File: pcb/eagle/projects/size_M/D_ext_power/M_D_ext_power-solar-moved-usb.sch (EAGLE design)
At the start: 30 parts

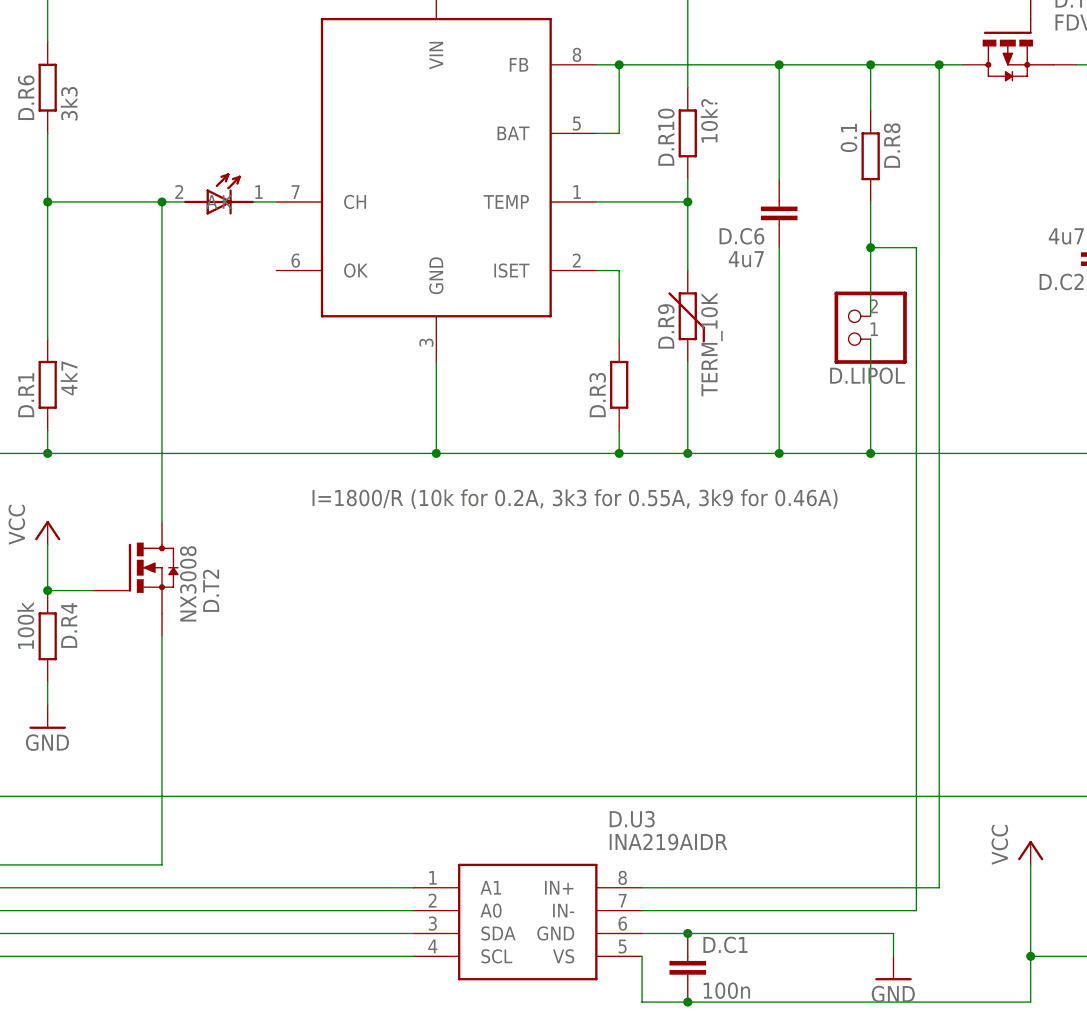
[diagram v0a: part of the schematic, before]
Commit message: LM3671_3.3 -> MCP1603T-330I attempt with  centered USB
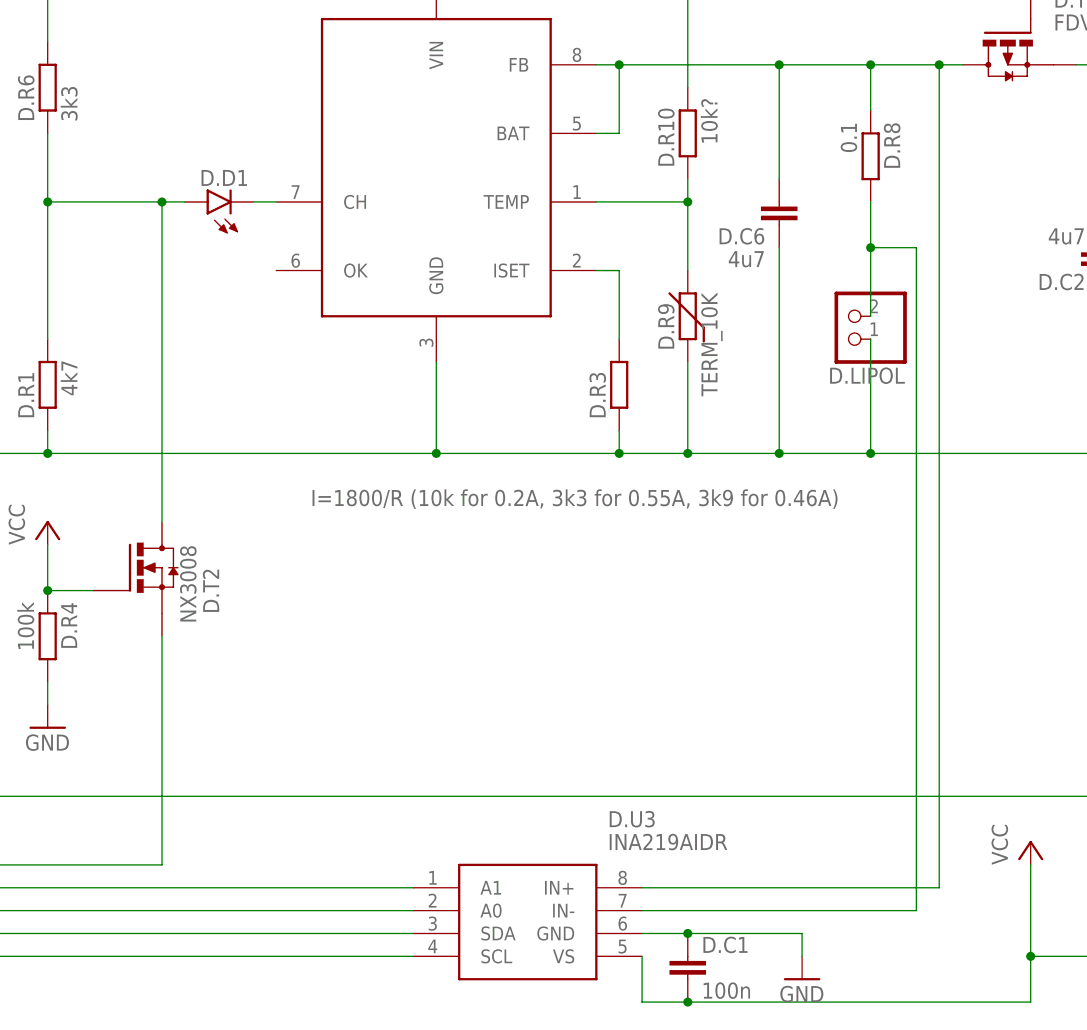
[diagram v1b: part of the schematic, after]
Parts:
- D.D1: value LED_1.8 -> (none); device hugo:LED_1.8 -> led:LEDCHIP-LED0603
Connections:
- net N$3: now also D.D1.C; no longer D.D1.K
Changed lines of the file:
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@@
 <part name="D.R6" library="rcl" library_urn="urn:adsk.eagle:library:334" deviceset="R-EU_" device="R0603" package3d_urn="urn:adsk.eagle:package:23555/3" value="3k3"/>
 <part name="D.R7" library="rcl" library_urn="urn:adsk.eagle:library:334" deviceset="R-EU_" device="R0603" package3d_urn="urn:adsk.eagle:package:23555/3" value="390k"/>
-<part name="D.D1" library="hugo" deviceset="LED_1.8" device=""/>
 <part name="D.L1" library="rcl" library_urn="urn:adsk.eagle:library:334" deviceset="L-EU" device="L3230M" package3d_urn="urn:adsk.eagle:package:23481/3" value="4u7"/>
 <part name="D.LIPOL" library="pinhead2" deviceset="PINHD-1X2" device="" package3d_urn="urn:adsk.eagle:package:22435/2"/>
@@
 <part name="U$2" library="hugo" deviceset="CN3083" device=""/>
 <part name="D.R10" library="rcl" library_urn="urn:adsk.eagle:library:334" deviceset="R-EU_" device="R0603" package3d_urn="urn:adsk.eagle:package:23555/3" value="10k?"/>
+<part name="D.D1" library="led" deviceset="LED" device="CHIP-LED0603" package3d_urn="urn:adsk.eagle:package:15819/3"/>
 </parts>
 <sheets>
@@
 <attribute name="VALUE" x="17.018" y="204.47" size="1.778" layer="96" rot="R270"/>
 </instance>
-<instance part="D.D1" gate="G$1" x="-88.9" y="190.5" smashed="yes"/>
 <instance part="D.L1" gate="G$1" x="71.12" y="205.74" smashed="yes" rot="R90">
 <attribute name="NAME" x="74.93" y="204.2414" size="1.778" layer="95" rot="R180"/>
@@
 <attribute name="VALUE" x="-111.76" y="129.54" size="1.778" layer="96"/>
 </instance>
-<instance part="GND5" gate="1" x="-15.24" y="104.14" smashed="yes">
-<attribute name="VALUE" x="-17.78" y="101.6" size="1.778" layer="96"/>
+<instance part="GND5" gate="1" x="-25.4" y="104.14" smashed="yes">
+<attribute name="VALUE" x="-27.94" y="101.6" size="1.778" layer="96"/>
 </instance>
 <instance part="U$2" gate="G$1" x="-68.58" y="198.12" smashed="yes">
@@
 <attribute name="NAME" x="-39.5986" y="194.31" size="1.778" layer="95" rot="R90"/>
 <attribute name="VALUE" x="-34.798" y="196.85" size="1.778" layer="96" rot="R90"/>
+</instance>
+<instance part="D.D1" gate="G$1" x="-91.44" y="190.5" smashed="yes" rot="R90">
+<attribute name="NAME" x="-86.868" y="194.056" size="1.778" layer="95" rot="R180"/>
+<attribute name="VALUE" x="-86.868" y="196.215" size="1.778" layer="96" rot="R180"/>
 </instance>
 </instances>
@@
 <pinref part="D.C1" gate="G$1" pin="1"/>
 <junction x="-38.1" y="109.22"/>
-<wire x1="-38.1" y1="109.22" x2="-15.24" y2="109.22" width="0.1524" layer="91"/>
+<wire x1="-38.1" y1="109.22" x2="-25.4" y2="109.22" width="0.1524" layer="91"/>
 <pinref part="GND5" gate="1" pin="GND"/>
-<wire x1="-15.24" y1="106.68" x2="-15.24" y2="109.22" width="0.1524" layer="91"/>
+<wire x1="-25.4" y1="106.68" x2="-25.4" y2="109.22" width="0.1524" layer="91"/>
 </segment>
 <segment>
@@
 <wire x1="-109.22" y1="190.5" x2="-109.22" y2="198.12" width="0.1524" layer="91"/>
 <junction x="-109.22" y="190.5"/>
-<pinref part="D.D1" gate="G$1" pin="A"/>
-<wire x1="-93.98" y1="190.5" x2="-96.52" y2="190.5" width="0.1524" layer="91"/>
 <pinref part="D.T2" gate="G$1" pin="D"/>
 <wire x1="-96.52" y1="154.94" x2="-96.52" y2="190.5" width="0.1524" layer="91"/>
 <junction x="-96.52" y="190.5"/>
 <wire x1="-109.22" y1="190.5" x2="-96.52" y2="190.5" width="0.1524" layer="91"/>
+<pinref part="D.D1" gate="G$1" pin="A"/>
+<wire x1="-96.52" y1="190.5" x2="-93.98" y2="190.5" width="0.1524" layer="91"/>
 </segment>
 </net>
@@
 <net name="N$3" class="0">
 <segment>
-<pinref part="D.D1" gate="G$1" pin="K"/>
 <pinref part="U$2" gate="G$1" pin="CH"/>
 <wire x1="-86.36" y1="190.5" x2="-83.82" y2="190.5" width="0.1524" layer="91"/>
-</segment>
-</net>
+<pinref part="D.D1" gate="G$1" pin="C"/>
+</segment>
+</net>
